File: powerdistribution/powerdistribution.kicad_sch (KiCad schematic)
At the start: 143 parts, among them IC1 NCP718ASNADJT1G, J1 282837-2, J2 282837-2, J3 ESQ-113-12-G-D, J6 Conn_01x02, M1 Motor_Servo, M2 Motor_Servo, Q1 IRLML0030, Q2 IRLML0030, Q3 IRLML0030, Q5 IRLML0030, U1 BQ7790512PW, U10 TPS1HC30BQPWPRQ1, U2 AP64501QSP-13, U3 AP64501QSP-13, U4 AP64501QSP-13, U5 TPS1HC30BQPWPRQ1, U6 TPS1HC30BQPWPRQ1, U7 ESP32-DEVKIT-V1, U8 LD1117S50TR_SOT223, U9 MIC29302AWD-TR

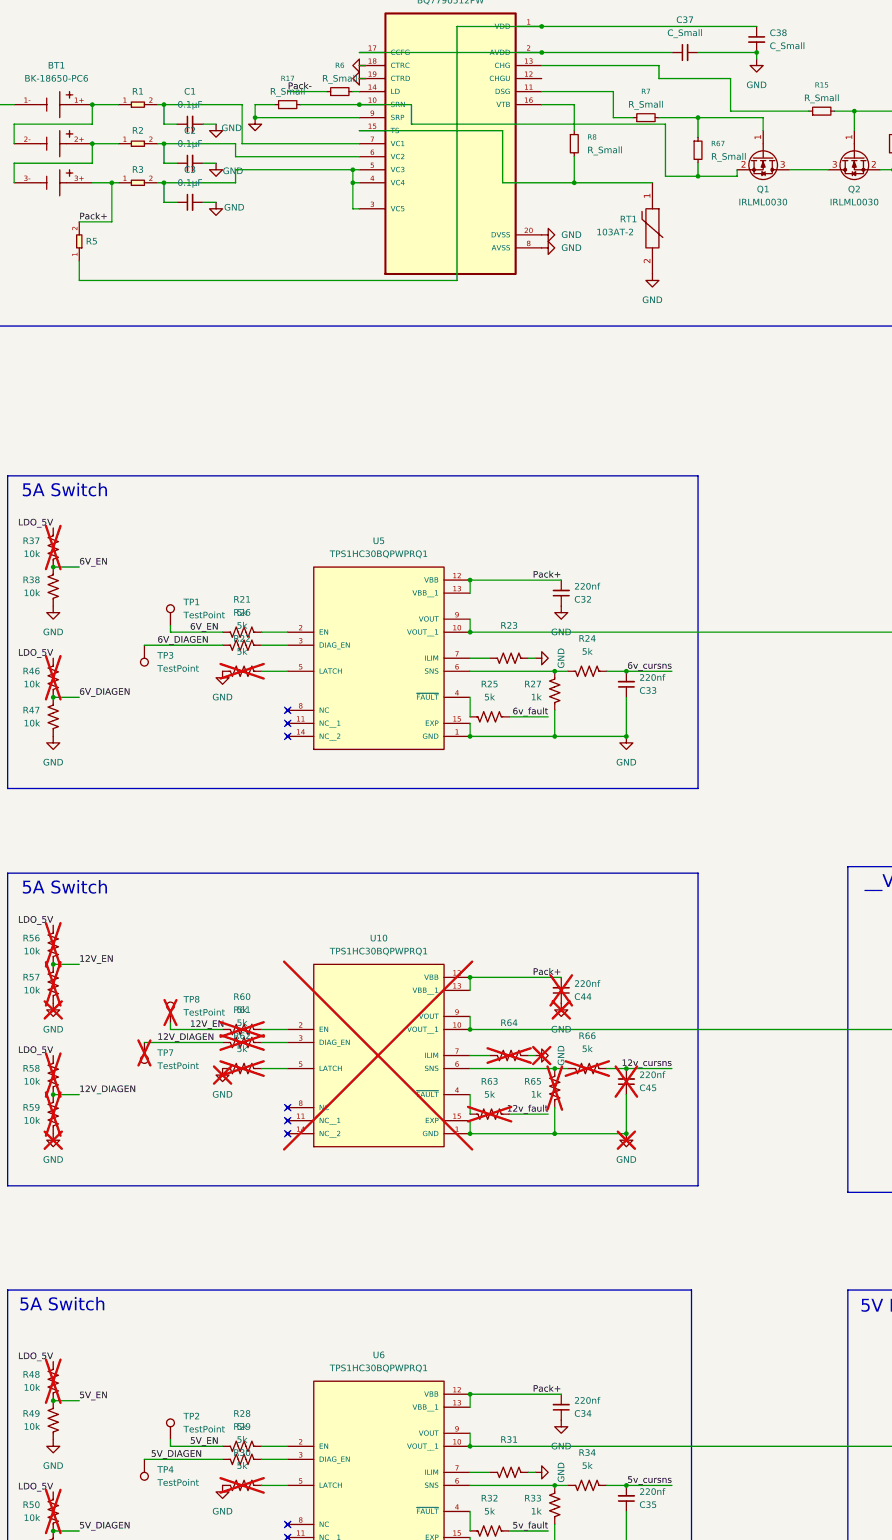
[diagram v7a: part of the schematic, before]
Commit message: power board placed and routed except connector, increased board length by 5mm
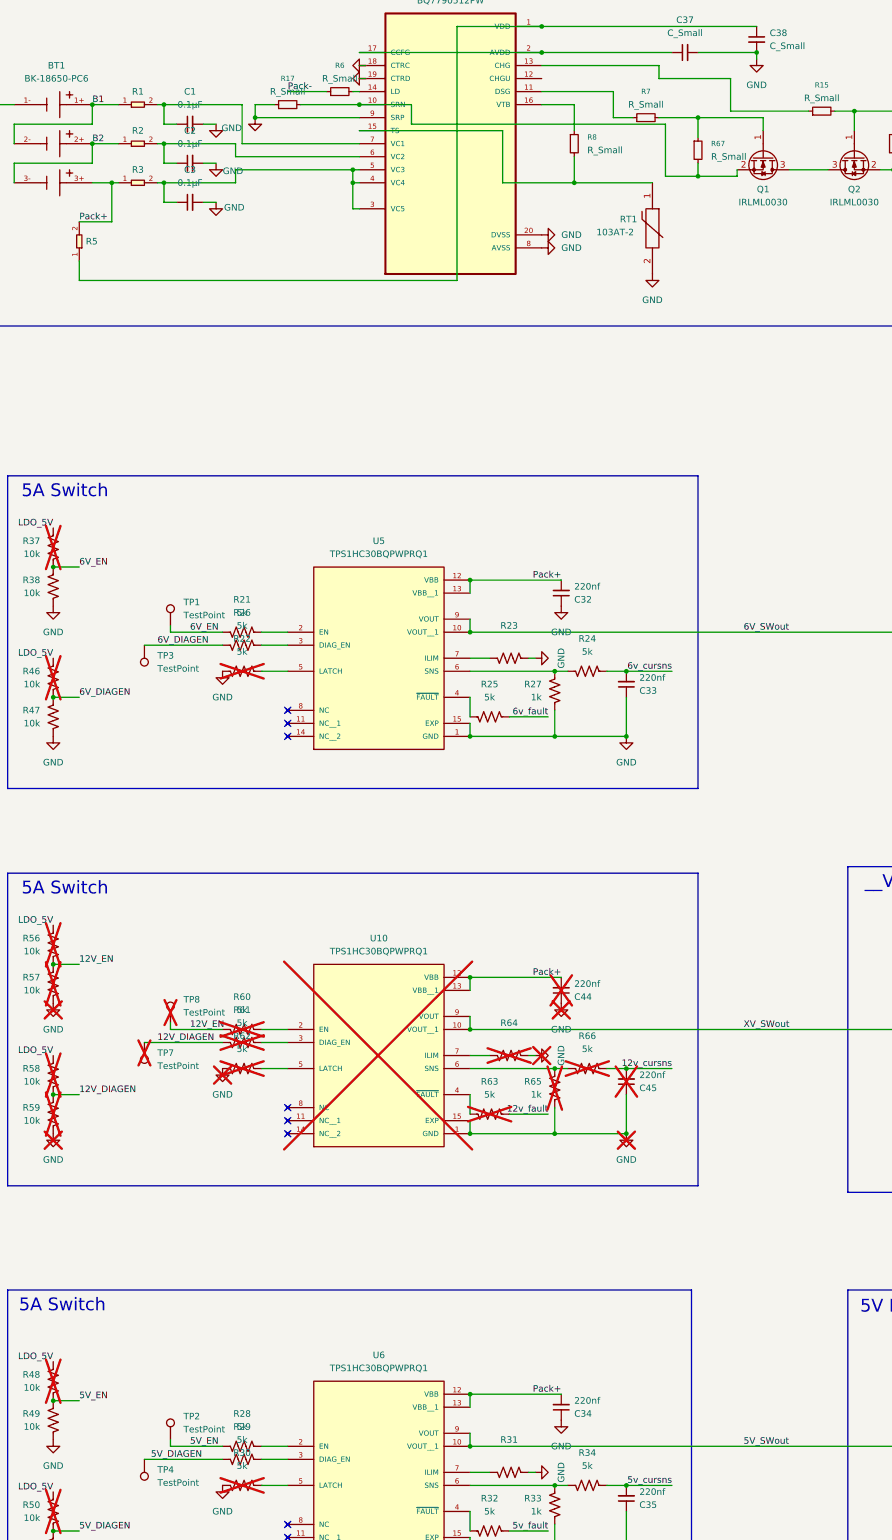
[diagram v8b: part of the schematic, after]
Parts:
- TP1, TP2, TP3, TP4, TP7, TP8: footprint Connector_PinHeader_2.00mm:PinHeader_1x01_P2.00mm_Vertical -> TestPoint:TestPoint_Pad_D2.0mm
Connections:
- net B1: now reaches BT1.1+, BT1.2-, R1.1
- net B2: now reaches BT1.2+, BT1.3-, R2.1
- net XV_SWout: now reaches C11.2, C5.2, U10.10 (VOUT__1), U10.9 (VOUT), U3.2 (VIN), U3.3 (EN)
- net 6V_SWout: now reaches C40.1, U5.10 (VOUT__1), U5.9 (VOUT), U9.1 (EN), U9.2 (IN)
- net 5V_SWout: now reaches C21.2, C22.2, U4.2 (VIN), U4.3 (EN), U6.10 (VOUT__1), U6.9 (VOUT)
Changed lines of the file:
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@@
 		)
 	)
+	(label "6V_SWout"
+		(at 185.42 167.64 0)
+		(effects
+			(font
+				(size 1.27 1.27)
+			)
+			(justify left bottom)
+		)
+	)
 	(label "5V"
 		(at 459.74 157.48 180)
@@
 		)
 	)
+	(label "B2"
+		(at 58.42 72.39 0)
+		(effects
+			(font
+				(size 1.27 1.27)
+			)
+			(justify left bottom)
+		)
+	)
 	(label "LDO_5V"
 		(at 50.8 224.79 180)
@@
 		)
 	)
+	(label "5V_SWout"
+		(at 185.42 326.39 0)
+		(effects
+			(font
+				(size 1.27 1.27)
+			)
+			(justify left bottom)
+		)
+	)
 	(label "6V_EN"
 		(at 55.88 154.94 0)
@@
 		)
 	)
+	(label "XV_SWout"
+		(at 185.42 245.11 0)
+		(effects
+			(font
+				(size 1.27 1.27)
+			)
+			(justify left bottom)
+		)
+	)
 	(label "6v_fault"
 		(at 448.31 204.47 180)
@@
 		)
 	)
+	(label "B1"
+		(at 58.42 64.77 0)
+		(effects
+			(font
+				(size 1.27 1.27)
+			)
+			(justify left bottom)
+		)
+	)
 	(label "LDO_5V"
 		(at 50.8 309.88 180)
@@
 			)
 		)
-		(property "Footprint" "Connector_PinHeader_2.00mm:PinHeader_1x01_P2.00mm_Vertical"
+		(property "Footprint" "TestPoint:TestPoint_Pad_D2.0mm"
 			(at 78.74 243.84 0)
 			(effects
@@
 			)
 		)
-		(property "Footprint" "Connector_PinHeader_2.00mm:PinHeader_1x01_P2.00mm_Vertical"
+		(property "Footprint" "TestPoint:TestPoint_Pad_D2.0mm"
 			(at 78.74 325.12 0)
 			(effects
@@
 			)
 		)
-		(property "Footprint" "Connector_PinHeader_2.00mm:PinHeader_1x01_P2.00mm_Vertical"
+		(property "Footprint" "TestPoint:TestPoint_Pad_D2.0mm"
 			(at 63.5 247.65 0)
 			(effects
@@
 			)
 		)
-		(property "Footprint" "Connector_PinHeader_2.00mm:PinHeader_1x01_P2.00mm_Vertical"
+		(property "Footprint" "TestPoint:TestPoint_Pad_D2.0mm"
 			(at 63.5 170.18 0)
 			(effects
@@
 			)
 		)
-		(property "Footprint" "Connector_PinHeader_2.00mm:PinHeader_1x01_P2.00mm_Vertical"
+		(property "Footprint" "TestPoint:TestPoint_Pad_D2.0mm"
 			(at 78.74 166.37 0)
 			(effects
@@
 			)
 		)
-		(property "Footprint" "Connector_PinHeader_2.00mm:PinHeader_1x01_P2.00mm_Vertical"
+		(property "Footprint" "TestPoint:TestPoint_Pad_D2.0mm"
 			(at 63.5 328.93 0)
 			(effects
